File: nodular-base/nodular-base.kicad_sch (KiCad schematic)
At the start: 30 parts, among them J11 Conn_01x08_Pin, SW1 SW_Push, SW2 SW_Push, SW3 SW_Push, U1 ESP32-S3-PICO-1-N8R2

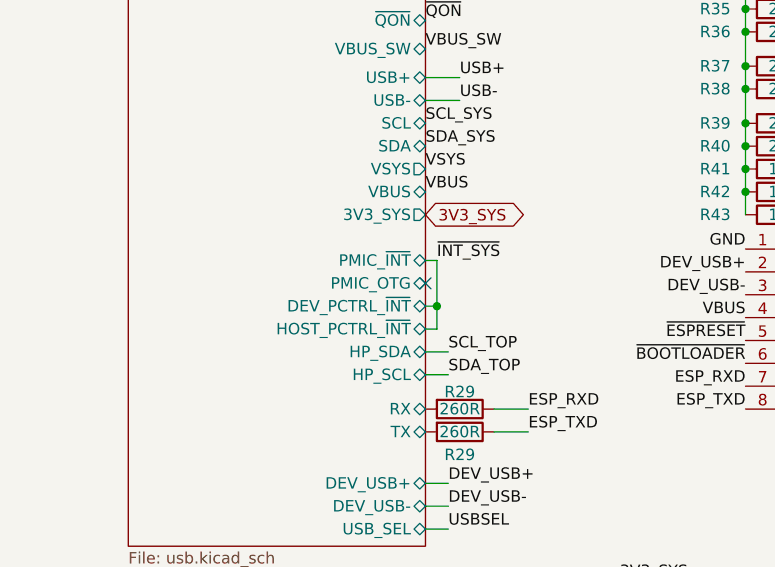
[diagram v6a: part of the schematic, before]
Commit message: Add 3d models and fix erc errors
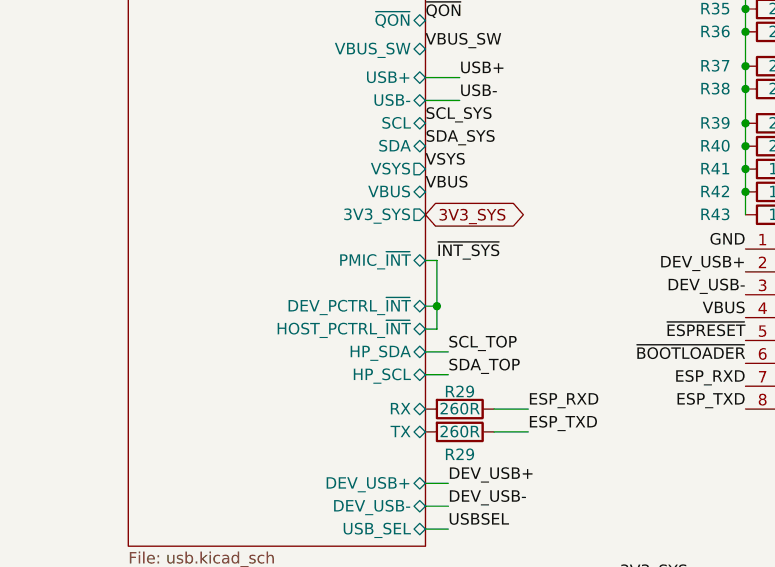
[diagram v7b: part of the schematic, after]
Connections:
- no-connect marks 2 -> 1
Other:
- sheet USB ports: added none; removed PMIC_OTG
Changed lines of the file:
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@@
   (junction (at 71.12 99.06) (diameter 0) (color 0 0 0 0)
   )
-  (no_connect (at 54.61 53.34))
   (no_connect (at 93.98 175.26))
   (wire (pts (xy 156.21 91.44) (xy 157.48 91.44))
@@
       (effects (font (size 1.27 1.27)) (justify right))
     )
-    (pin "PMIC_OTG" bidirectional (at 54.61 53.34 0)
-      (effects (font (size 1.27 1.27)) (justify right))
-    )

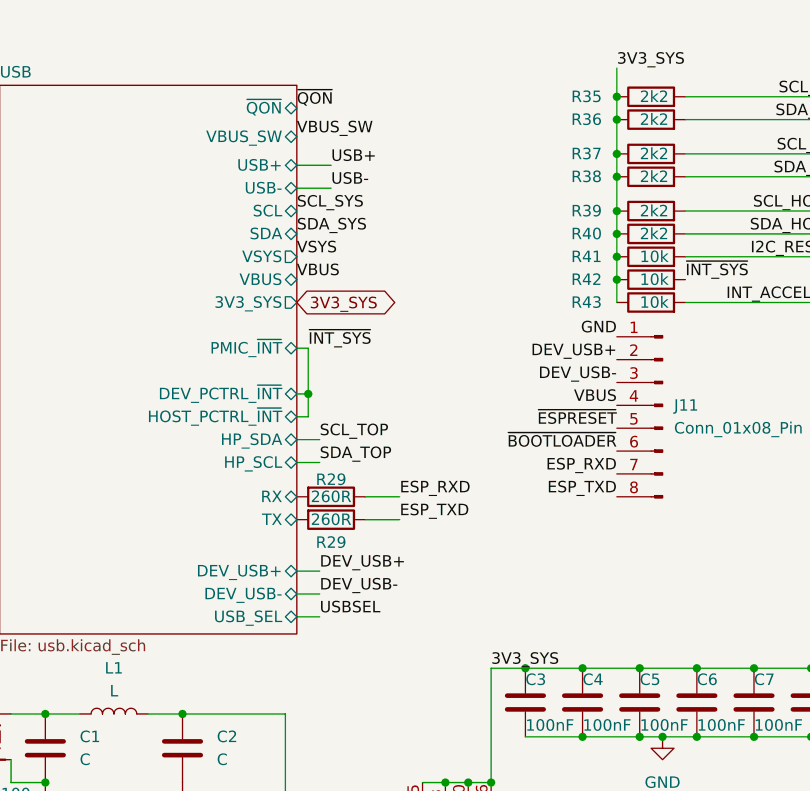
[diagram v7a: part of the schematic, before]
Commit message: Add additional accelerometer-gyro option, update pin and address map, fix some ERC errors
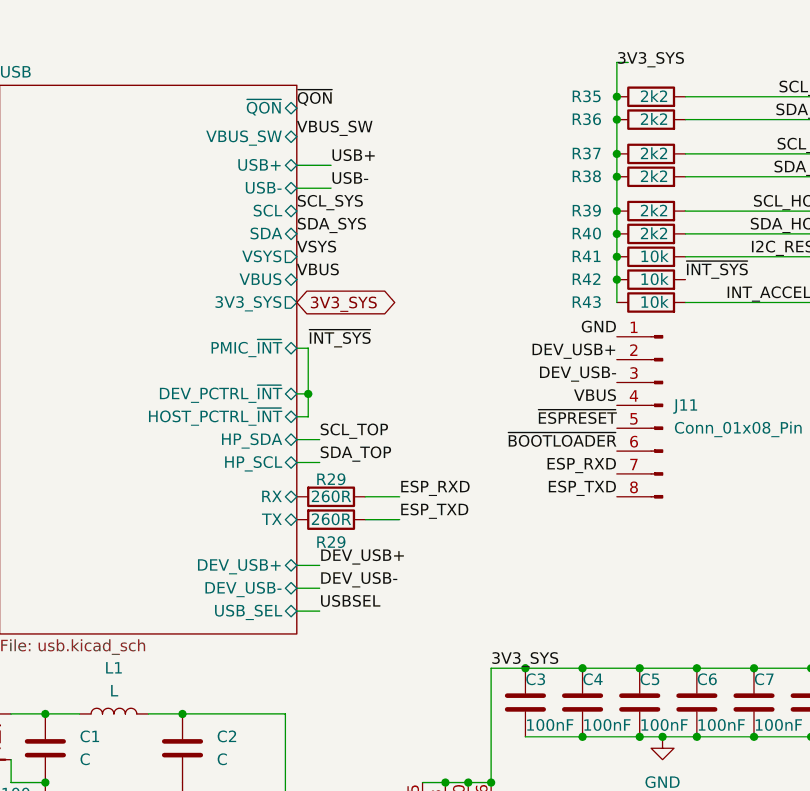
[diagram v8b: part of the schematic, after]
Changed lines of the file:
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@@
+    (stroke (width 0) (type default))
+  )
+  (wire (pts (xy 91.44 19.05) (xy 90.17 19.05))
     (stroke (width 0) (type default))
   )
@@
     (stroke (width 0) (type default))
   )
-  (wire (pts (xy 90.17 19.685) (xy 90.17 22.86))
-    (stroke (width 0) (type default))
-  )
   (wire (pts (xy 184.15 144.78) (xy 205.74 144.78))
     (stroke (width 0) (type default))
@@
     (stroke (width 0) (type default))
   )
-  (wire (pts (xy 54.61 80.645) (xy 57.15 80.645))
+  (wire (pts (xy 54.61 80.01) (xy 57.15 80.01))
     (stroke (width 0) (type default))
   )
@@
     (stroke (width 0) (type default))
   )
-  (wire (pts (xy 54.61 75.565) (xy 57.15 75.565))
+  (wire (pts (xy 54.61 74.93) (xy 57.15 74.93))
     (stroke (width 0) (type default))
   )
@@
     (stroke (width 0) (type default))
   )
+  (wire (pts (xy 90.17 19.05) (xy 90.17 22.86))
+    (stroke (width 0) (type default))
+  )
   (wire (pts (xy 185.42 82.55) (xy 205.74 82.55))
     (stroke (width 0) (type default))
@@
     (stroke (width 0) (type default))
   )
-  (wire (pts (xy 54.61 78.105) (xy 57.15 78.105))
+  (wire (pts (xy 54.61 77.47) (xy 57.15 77.47))
     (stroke (width 0) (type default))
   )
@@
     (stroke (width 0) (type default))
   )
-  (label "DEV_USB+" (at 57.15 75.565 0) (fields_autoplaced)
+  (label "DEV_USB+" (at 57.15 74.93 0) (fields_autoplaced)
     (effects (font (size 1.27 1.27)) (justify left bottom))
   )
@@
     (effects (font (size 1.27 1.27)) (justify left bottom))
   )
-  (label "USBSEL" (at 57.15 80.645 0) (fields_autoplaced)
+  (label "USBSEL" (at 57.15 80.01 0) (fields_autoplaced)
     (effects (font (size 1.27 1.27)) (justify left bottom))
   )
@@
     (effects (font (size 1.27 1.27)) (justify right bottom))
   )
-  (label "DEV_USB-" (at 57.15 78.105 0) (fields_autoplaced)
+  (label "DEV_USB-" (at 57.15 77.47 0) (fields_autoplaced)
     (effects (font (size 1.27 1.27)) (justify left bottom))
   )
@@
       (effects (font (size 1.27 1.27)) (justify right))
     )
-    (pin "DEV_USB+" bidirectional (at 54.61 75.565 0)
-      (effects (font (size 1.27 1.27)) (justify right))
-    )
-    (pin "DEV_USB-" bidirectional (at 54.61 78.105 0)
-      (effects (font (size 1.27 1.27)) (justify right))
-    )
-    (pin "USB_SEL" bidirectional (at 54.61 80.645 0)
-      (effects (font (size 1.27 1.27)) (justify right))
-    )
+    (pin "DEV_USB+" bidirectional (at 54.61 74.93 0)
+      (effects (font (size 1.27 1.27)) (justify right))
+    )
+    (pin "DEV_USB-" bidirectional (at 54.61 77.47 0)
+      (effects (font (size 1.27 1.27)) (justify right))
+    )
+    (pin "USB_SEL" bidirectional (at 54.61 80.01 0)
+      (effects (font (size 1.27 1.27)) (justify right))
+    )
